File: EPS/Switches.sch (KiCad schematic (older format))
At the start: 13 parts

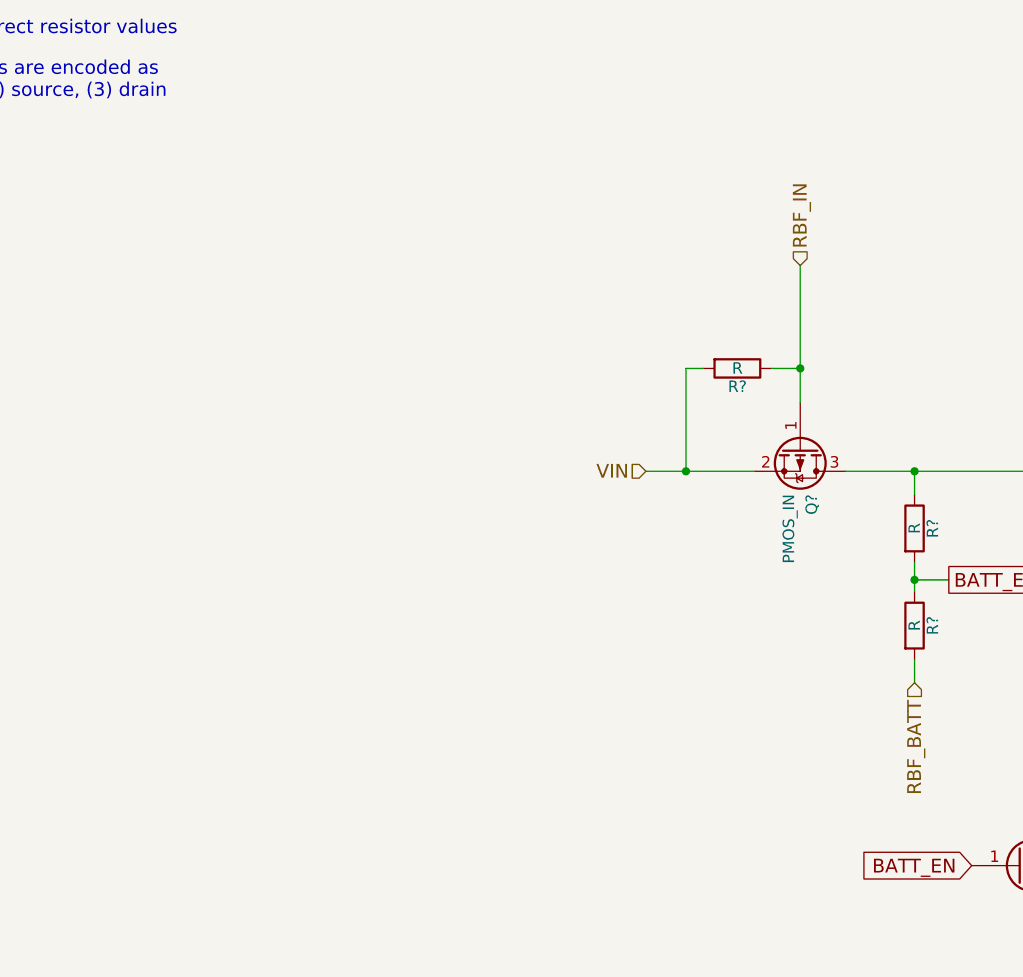
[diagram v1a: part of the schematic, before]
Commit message: Updated Schematics
Added:
- digital pot
- digital loads
- updated  switch sheet to block two ways before battery
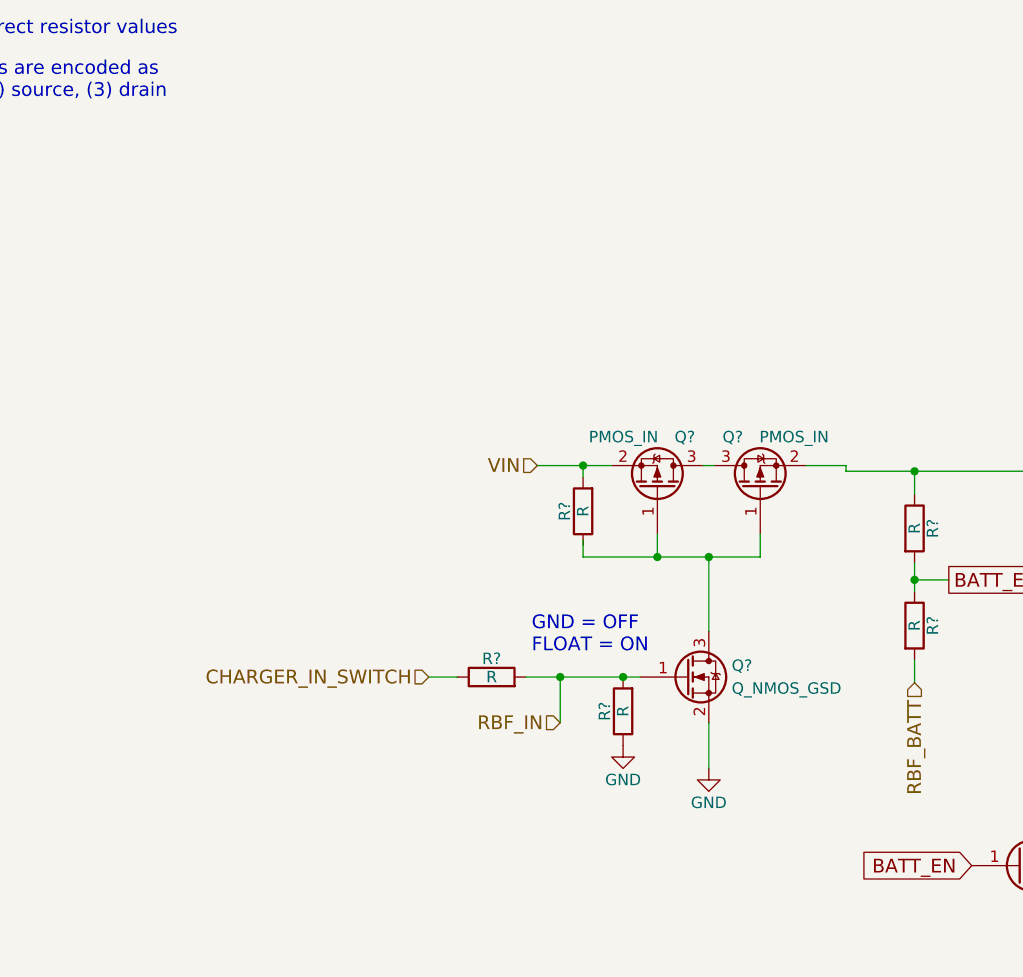
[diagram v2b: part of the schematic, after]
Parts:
- added Q?: PMOS_IN, symbol Q_PMOS_GSD
- added Q?: Q_NMOS_GSD, symbol Q_NMOS_GSD
- added R? (x2): R, symbol R
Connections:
- net BATT+: now also Q?.2 (S); no longer Q?.3 (D)
- net GND: now also Q?.2 (S), R?.1
- net RBF_IN: now also Q?.1 (G), R?.2, R?.2; no longer Q?.1 (G), R?.1
- new net: Q?.1 (G), Q?.1 (G), Q?.3 (D)
- new net: Q?.3 (D), Q?.3 (D)
- new net CHARGER_IN_SWITCH: R?.1
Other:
- note added: "GND = OFF\nFLOAT = ON"
- moved on the sheet: Q?, R?
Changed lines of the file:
@@
 LIBS:tps7a7002
 LIBS:max5395
+LIBS:ina210
+LIBS:ncs20071
 LIBS:EPS-cache
 EELAYER 25 0
@@
 $Descr A4 11693 8268
 encoding utf-8
-Sheet 8 13
+Sheet 9 14
 Title "Switches"
 Date "2018-02-15"
@@
 L Q_PMOS_GSD Q?
 U 1 1 5A8D722B
-P 4825 3350
-F 0 "Q?" H 5025 3400 50  0000 L CNN
-F 1 "PMOS_IN" H 5025 3300 50  0000 L CNN
-F 2 "" H 5025 3450 50  0001 C CNN
-F 3 "" H 4825 3350 50  0001 C CNN
-	1    4825 3350
-	0    1    1    0
-$EndComp
-Text HLabel 4150 3450 0    60   Input ~ 0
+P 4200 3525
+F 0 "Q?" V 4425 3600 50  0000 L CNN
+F 1 "PMOS_IN" V 4425 3225 50  0000 L CNN
+F 2 "" H 4400 3625 50  0001 C CNN
+F 3 "" H 4200 3525 50  0001 C CNN
+	1    4200 3525
+	0    1    -1   0
+$EndComp
+Text HLabel 3675 3425 0    60   Input ~ 0
 VIN
-Wire Wire Line
-	4150 3450 4625 3450
 $Comp
 L R R?
 U 1 1 5A8D7B52
-P 4550 3000
-F 0 "R?" V 4630 3000 50  0000 C CNN
-F 1 "R" V 4550 3000 50  0000 C CNN
-F 2 "" V 4480 3000 50  0001 C CNN
-F 3 "" H 4550 3000 50  0001 C CNN
-	1    4550 3000
-	0    1    1    0
-$EndComp
-Wire Wire Line
-	4400 3000 4325 3000
-Wire Wire Line
-	4325 3000 4325 3450
-Connection ~ 4325 3450
-Wire Wire Line
-	4700 3000 4825 3000
-Wire Wire Line
-	4825 2550 4825 3150
-Text HLabel 4825 2550 1    60   Input ~ 0
+P 3875 3625
+F 0 "R?" V 3955 3625 50  0000 C CNN
+F 1 "R" V 3875 3625 50  0000 C CNN
+F 2 "" V 3805 3625 50  0001 C CNN
+F 3 "" H 3875 3625 50  0001 C CNN
+	1    3875 3625
+	-1   0    0    1
+$EndComp
+Text HLabel 3775 4550 0    60   Input ~ 0
 RBF_IN
-Connection ~ 4825 3000
 $Comp
 L Q_PMOS_GSD Q?
@@
 Text Notes 9025 2225 0    60   ~ 0
 GND => OFF\nFLOATING (high impedance) => ON
+$Comp
+L Q_PMOS_GSD Q?
+U 1 1 5A9064FD
+P 4650 3525
+F 0 "Q?" V 4875 3600 50  0000 L CNN
+F 1 "PMOS_IN" V 4875 3225 50  0000 L CNN
+F 2 "" H 4850 3625 50  0001 C CNN
+F 3 "" H 4650 3525 50  0001 C CNN
+	1    4650 3525
+	0    -1   -1   0
+$EndComp
+Wire Wire Line
+	4400 3425 4450 3425
+Wire Wire Line
+	3675 3425 4000 3425
+Wire Wire Line
+	3875 3425 3875 3475
+Connection ~ 3875 3425
+Wire Wire Line
+	3875 3750 3875 3825
+Wire Wire Line
+	3875 3825 4650 3825
+Wire Wire Line
+	4200 3825 4200 3725
+Wire Wire Line
+	4650 3825 4650 3725
+Connection ~ 4200 3825
+Wire Wire Line
+	4425 3825 4425 4150
+Connection ~ 4425 3825
+$Comp
+L Q_NMOS_GSD Q?
+U 1 1 5A906945
+P 4325 4350
+F 0 "Q?" H 4525 4400 50  0000 L CNN
+F 1 "Q_NMOS_GSD" H 4525 4300 50  0000 L CNN
+F 2 "" H 4525 4450 50  0001 C CNN
+F 3 "" H 4325 4350 50  0001 C CNN
+	1    4325 4350
+	1    0    0    -1
+$EndComp
+$Comp
+L GND #PWR?
+U 1 1 5A9069CB
+P 4425 4750
+F 0 "#PWR?" H 4425 4500 50  0001 C CNN
+F 1 "GND" H 4425 4600 50  0000 C CNN
+F 2 "" H 4425 4750 50  0001 C CNN
+F 3 "" H 4425 4750 50  0001 C CNN
+	1    4425 4750
+	1    0    0    -1
+$EndComp
+Wire Wire Line
+	4425 4750 4425 4550
+$Comp
+L R R?
+U 1 1 5A906AE1
+P 4050 4500
+F 0 "R?" V 4130 4500 50  0000 C CNN
+F 1 "R" V 4050 4500 50  0000 C CNN
+F 2 "" V 3980 4500 50  0001 C CNN
+F 3 "" H 4050 4500 50  0001 C CNN
+	1    4050 4500
+	-1   0    0    1
+$EndComp
+$Comp
+L R R?
+U 1 1 5A906B3F
+P 3475 4350
+F 0 "R?" V 3555 4350 50  0000 C CNN
+F 1 "R" V 3475 4350 50  0000 C CNN
+F 2 "" V 3405 4350 50  0001 C CNN
+F 3 "" H 3475 4350 50  0001 C CNN
+	1    3475 4350
+	0    -1   -1   0
+$EndComp
+Wire Wire Line
+	3625 4350 4125 4350
+Connection ~ 4050 4350
+$Comp
+L GND #PWR?
+U 1 1 5A906C2C
+P 4050 4650
+F 0 "#PWR?" H 4050 4400 50  0001 C CNN
+F 1 "GND" H 4050 4500 50  0000 C CNN
+F 2 "" H 4050 4650 50  0001 C CNN
+F 3 "" H 4050 4650 50  0001 C CNN
+	1    4050 4650
+	1    0    0    -1
+$EndComp
+Wire Wire Line
+	3775 4550 3775 4350
+Connection ~ 3775 4350
+Text HLabel 3200 4350 0    60   Input ~ 0
+CHARGER_IN_SWITCH
+Wire Wire Line
+	3200 4350 3325 4350
+Wire Wire Line
+	4850 3425 5025 3425
+Wire Wire Line
+	5025 3425 5025 3450
+Text Notes 3650 4250 0    60   ~ 0
+GND = OFF\nFLOAT = ON
 $EndSCHEMATC

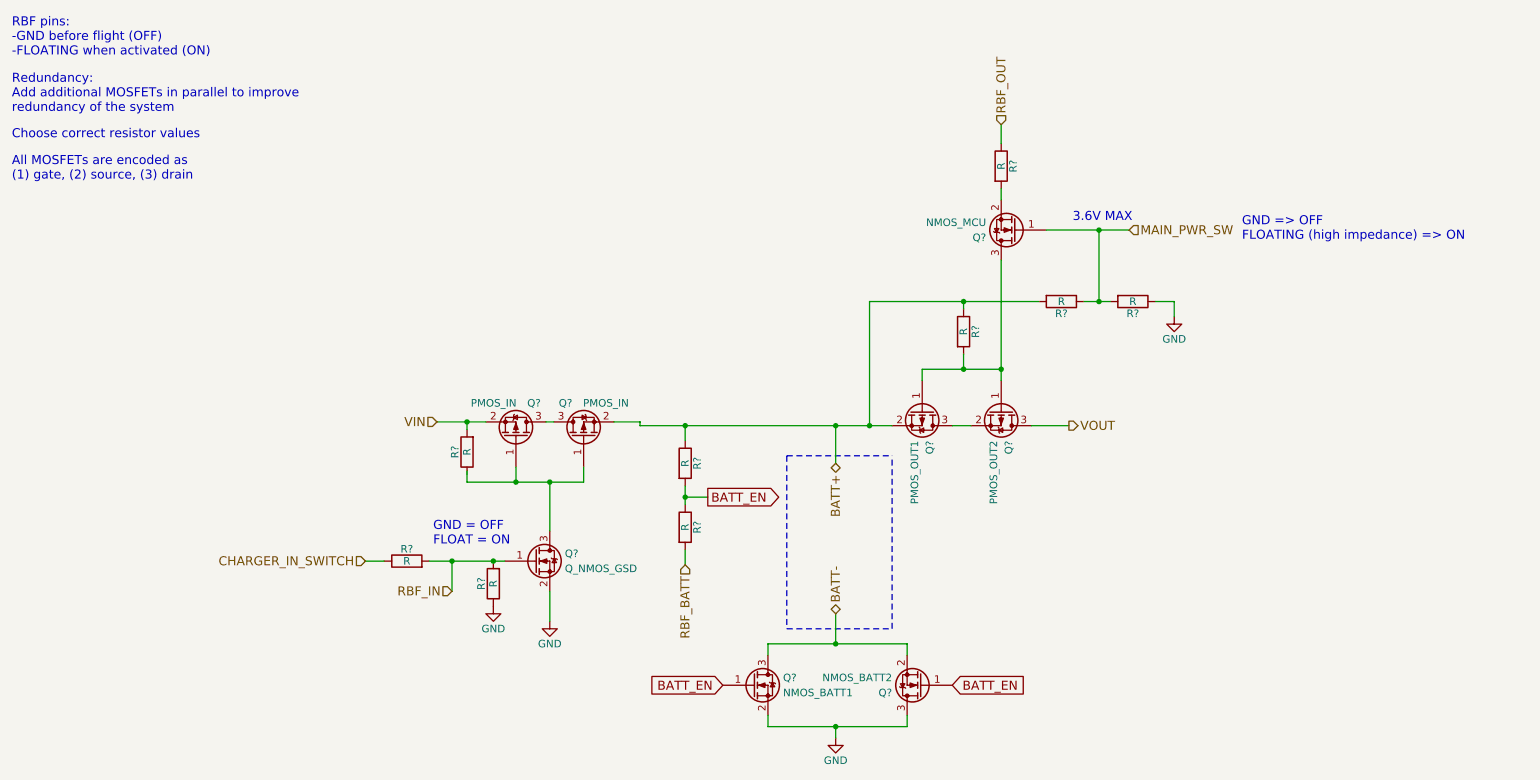
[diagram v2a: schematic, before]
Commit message: Finalized SCH (beta version) and started pcb
Capacitor banks might need to be reassigned to other locations.
No RBF pin on this SCH or PCB.
Battery gound deployment switch is fully mechanical (no mosfet switch on low side).
PCB of the prototype started. Main power converters and current measuring devices layed out.
SCH still requires ESD protection diodes!
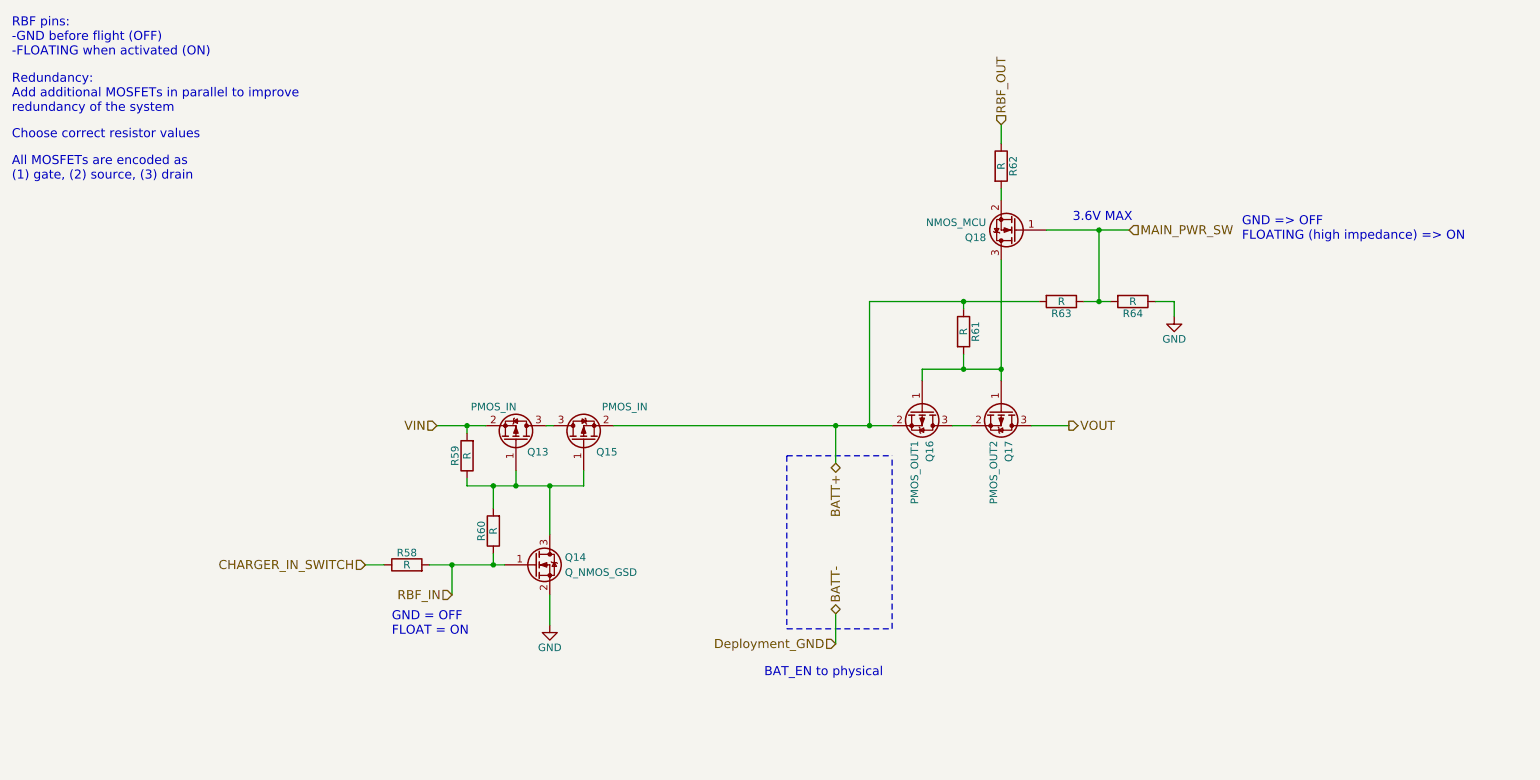
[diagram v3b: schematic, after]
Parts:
- removed Q?: NMOS_BATT1, symbol Q_NMOS_GSD
- removed Q?: NMOS_BATT2, symbol Q_NMOS_GSD
- removed R? (x3): R, symbol R
- added R60: R, Resistors_SMD:R_0603, symbol R
- Q13, Q14, Q15, Q16, Q17, Q18: renamed from Q?; footprint (none) -> TO_SOT_Packages_SMD:SOT-23
- R58, R59, R61, R62, R63, R64: renamed from R?; footprint (none) -> Resistors_SMD:R_0603
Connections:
- net RBF_IN: now also R60.1
- net at Q13.1 (G), Q14.3 (D), Q15.1 (G): now also R59.1, R60.2
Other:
- note added: "BAT_EN to physical\n"
- moved on the sheet: Q13, Q14, Q15, R58, R59
